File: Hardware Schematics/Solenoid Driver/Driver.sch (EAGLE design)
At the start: 6 parts

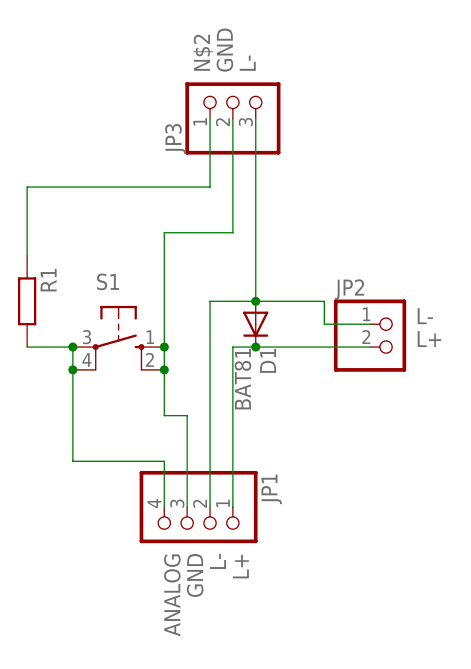
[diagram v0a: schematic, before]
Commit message: New Solenoid Driver Design
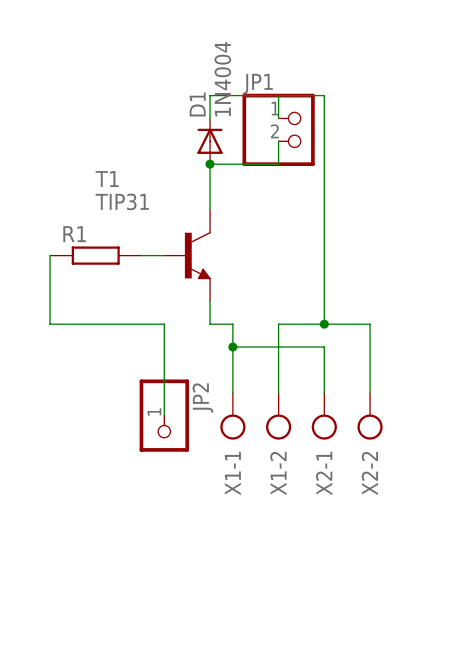
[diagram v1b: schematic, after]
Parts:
- removed JP3: (no value), pinhead:PINHD-1X3
- removed S1: (no value), switch-omron:10-XX
- added T1: TIP31, transistor:TIP31
- added X1, X2: (no value), con-ptr500:AK500/2-H
- D1: value BAT81 -> 1N4004; device diode:BAT81 -> diode:1N4004
- JP1: device pinhead:PINHD-1X4 -> pinhead:PINHD-1X2
- JP2: device pinhead:PINHD-1X2 -> pinhead:PINHD-1X1
- R1: device resistor:R-EU_0204/7 -> rcl:R-EU_0204/2V
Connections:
- removed net ANALOG: JP1.4, R1.2, S1.P, S1.P1
- removed net GND: JP1.3, JP3.2, S1.S, S1.S1
- removed net L+: D1.C, JP1.1, JP2.2
- removed net L-: D1.A, JP1.2, JP2.1, JP3.3
- new net N$1: D1.A, JP1.2, T1.C
- new net N$3: T1.E, X1-1.KL, X2-1.KL
- new net N$4: JP2.1, R1.1
- new net N$5: D1.C, JP1.1, X1-2.KL, X2-2.KL
- net N$2: now also R1.2, T1.B; no longer JP3.1, R1.1
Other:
- moved on the sheet: D1, R1
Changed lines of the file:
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@@
 </classes>
 <parts>
-<part name="S1" library="switch-omron" deviceset="10-XX" device=""/>
-<part name="R1" library="resistor" deviceset="R-EU_" device="0204/7"/>
-<part name="JP1" library="pinhead" deviceset="PINHD-1X4" device=""/>
-<part name="JP2" library="pinhead" deviceset="PINHD-1X2" device=""/>
-<part name="JP3" library="pinhead" deviceset="PINHD-1X3" device=""/>
-<part name="D1" library="diode" deviceset="BAT81" device=""/>
+<part name="T1" library="transistor" deviceset="TIP31" device=""/>
+<part name="R1" library="rcl" deviceset="R-EU_" device="0204/2V"/>
+<part name="D1" library="diode" deviceset="1N4004" device=""/>
+<part name="JP1" library="pinhead" deviceset="PINHD-1X2" device=""/>
+<part name="JP2" library="pinhead" deviceset="PINHD-1X1" device=""/>
+<part name="X1" library="con-ptr500" deviceset="AK500/2-H" device=""/>
+<part name="X2" library="con-ptr500" deviceset="AK500/2-H" device=""/>
 </parts>
 <sheets>
@@
 </plain>
 <instances>
-<instance part="S1" gate="1" x="-5.08" y="45.72" rot="R270"/>
-<instance part="R1" gate="G$1" x="-15.24" y="50.8" rot="R270"/>
-<instance part="JP1" gate="A" x="2.54" y="25.4" rot="R270"/>
-<instance part="JP2" gate="G$1" x="25.4" y="45.72"/>
-<instance part="JP3" gate="A" x="7.62" y="73.66" rot="R90"/>
-<instance part="D1" gate="1" x="10.16" y="48.26" rot="R270"/>
+<instance part="T1" gate="G$1" x="2.54" y="55.88"/>
+<instance part="R1" gate="G$1" x="-7.62" y="55.88"/>
+<instance part="D1" gate="1" x="5.08" y="68.58" rot="R90"/>
+<instance part="JP1" gate="G$1" x="15.24" y="68.58"/>
+<instance part="JP2" gate="G$1" x="0" y="35.56" rot="R270"/>
+<instance part="X1" gate="-1" x="7.62" y="35.56" rot="R90"/>
+<instance part="X1" gate="-2" x="12.7" y="35.56" rot="R90"/>
+<instance part="X2" gate="-1" x="17.78" y="35.56" rot="R90"/>
+<instance part="X2" gate="-2" x="22.86" y="35.56" rot="R90"/>
 </instances>
 <busses>
 </busses>
 <nets>
-<net name="ANALOG" class="0">
+<net name="N$1" class="0">
 <segment>
-<pinref part="R1" gate="G$1" pin="2"/>
-<pinref part="S1" gate="1" pin="P"/>
-<wire x1="-15.24" y1="45.72" x2="-10.16" y2="45.72" width="0.1524" layer="91"/>
-<pinref part="S1" gate="1" pin="P1"/>
-<wire x1="-10.16" y1="45.72" x2="-10.16" y2="43.18" width="0.1524" layer="91"/>
-<wire x1="-10.16" y1="43.18" x2="-10.16" y2="33.02" width="0.1524" layer="91"/>
-<pinref part="JP1" gate="A" pin="4"/>
-<wire x1="-10.16" y1="33.02" x2="0" y2="33.02" width="0.1524" layer="91"/>
-<wire x1="0" y1="33.02" x2="0" y2="27.94" width="0.1524" layer="91"/>
-<label x="0" y="22.86" size="1.778" layer="95" rot="R270"/>
-<junction x="-10.16" y="45.72"/>
-<junction x="-10.16" y="43.18"/>
+<pinref part="D1" gate="1" pin="A"/>
+<pinref part="T1" gate="G$1" pin="C"/>
+<wire x1="5.08" y1="66.04" x2="5.08" y2="60.96" width="0.1524" layer="91"/>
+<pinref part="JP1" gate="G$1" pin="2"/>
+<wire x1="12.7" y1="68.58" x2="12.7" y2="66.04" width="0.1524" layer="91"/>
+<wire x1="12.7" y1="66.04" x2="5.08" y2="66.04" width="0.1524" layer="91"/>
+<junction x="5.08" y="66.04"/>
 </segment>
 </net>
 <net name="N$2" class="0">
 <segment>
-<pinref part="R1" gate="G$1" pin="1"/>
-<wire x1="-15.24" y1="55.88" x2="-15.24" y2="63.5" width="0.1524" layer="91"/>
-<wire x1="-15.24" y1="63.5" x2="5.08" y2="63.5" width="0.1524" layer="91"/>
-<pinref part="JP3" gate="A" pin="1"/>
-<wire x1="5.08" y1="63.5" x2="5.08" y2="71.12" width="0.1524" layer="91"/>
-<label x="5.08" y="76.2" size="1.778" layer="95" rot="R90"/>
+<pinref part="R1" gate="G$1" pin="2"/>
+<pinref part="T1" gate="G$1" pin="B"/>
+<wire x1="-2.54" y1="55.88" x2="0" y2="55.88" width="0.1524" layer="91"/>
 </segment>
 </net>
-<net name="GND" class="0">
+<net name="N$5" class="0">
 <segment>
-<pinref part="S1" gate="1" pin="S"/>
-<pinref part="S1" gate="1" pin="S1"/>
-<wire x1="0" y1="45.72" x2="0" y2="43.18" width="0.1524" layer="91"/>
-<wire x1="0" y1="43.18" x2="0" y2="38.1" width="0.1524" layer="91"/>
-<pinref part="JP1" gate="A" pin="3"/>
-<wire x1="0" y1="38.1" x2="2.54" y2="38.1" width="0.1524" layer="91"/>
-<wire x1="2.54" y1="38.1" x2="2.54" y2="27.94" width="0.1524" layer="91"/>
-<wire x1="0" y1="45.72" x2="0" y2="58.42" width="0.1524" layer="91"/>
-<pinref part="JP3" gate="A" pin="2"/>
-<wire x1="0" y1="58.42" x2="7.62" y2="58.42" width="0.1524" layer="91"/>
-<wire x1="7.62" y1="58.42" x2="7.62" y2="71.12" width="0.1524" layer="91"/>
-<label x="2.54" y="22.86" size="1.778" layer="95" rot="R270"/>
-<label x="7.62" y="76.2" size="1.778" layer="95" rot="R90"/>
-<junction x="0" y="45.72"/>
-<junction x="0" y="43.18"/>
+<pinref part="D1" gate="1" pin="C"/>
+<wire x1="5.08" y1="71.12" x2="5.08" y2="73.66" width="0.1524" layer="91"/>
+<wire x1="5.08" y1="73.66" x2="12.7" y2="73.66" width="0.1524" layer="91"/>
+<wire x1="12.7" y1="73.66" x2="12.7" y2="71.12" width="0.1524" layer="91"/>
+<pinref part="JP1" gate="G$1" pin="1"/>
+<wire x1="12.7" y1="73.66" x2="17.78" y2="73.66" width="0.1524" layer="91"/>
+<wire x1="17.78" y1="73.66" x2="17.78" y2="48.26" width="0.1524" layer="91"/>
+<wire x1="17.78" y1="48.26" x2="12.7" y2="48.26" width="0.1524" layer="91"/>
+<pinref part="X1" gate="-2" pin="KL"/>
+<wire x1="12.7" y1="48.26" x2="12.7" y2="40.64" width="0.1524" layer="91"/>
+<wire x1="17.78" y1="48.26" x2="22.86" y2="48.26" width="0.1524" layer="91"/>
+<pinref part="X2" gate="-2" pin="KL"/>
+<wire x1="22.86" y1="48.26" x2="22.86" y2="40.64" width="0.1524" layer="91"/>
+<junction x="17.78" y="48.26"/>
 </segment>
 </net>
-<net name="L-" class="0">
+<net name="N$4" class="0">
 <segment>
-<pinref part="JP1" gate="A" pin="2"/>
-<wire x1="5.08" y1="27.94" x2="5.08" y2="50.8" width="0.1524" layer="91"/>
-<pinref part="D1" gate="1" pin="A"/>
-<wire x1="5.08" y1="50.8" x2="10.16" y2="50.8" width="0.1524" layer="91"/>
+<pinref part="R1" gate="G$1" pin="1"/>
+<wire x1="-12.7" y1="55.88" x2="-12.7" y2="48.26" width="0.1524" layer="91"/>
+<wire x1="-12.7" y1="48.26" x2="0" y2="48.26" width="0.1524" layer="91"/>
 <pinref part="JP2" gate="G$1" pin="1"/>
-<wire x1="22.86" y1="48.26" x2="17.78" y2="48.26" width="0.1524" layer="91"/>
-<wire x1="17.78" y1="48.26" x2="17.78" y2="50.8" width="0.1524" layer="91"/>
-<wire x1="17.78" y1="50.8" x2="10.16" y2="50.8" width="0.1524" layer="91"/>
-<pinref part="JP3" gate="A" pin="3"/>
-<wire x1="10.16" y1="71.12" x2="10.16" y2="50.8" width="0.1524" layer="91"/>
-<label x="27.94" y="48.26" size="1.778" layer="95"/>
-<label x="5.08" y="22.86" size="1.778" layer="95" rot="R270"/>
-<label x="10.16" y="76.2" size="1.778" layer="95" rot="R90"/>
-<junction x="10.16" y="50.8"/>
+<wire x1="0" y1="48.26" x2="0" y2="38.1" width="0.1524" layer="91"/>
 </segment>
 </net>
-<net name="L+" class="0">
+<net name="N$3" class="0">
 <segment>
-<pinref part="JP1" gate="A" pin="1"/>
-<wire x1="7.62" y1="27.94" x2="7.62" y2="45.72" width="0.1524" layer="91"/>
-<pinref part="D1" gate="1" pin="C"/>
-<wire x1="7.62" y1="45.72" x2="10.16" y2="45.72" width="0.1524" layer="91"/>
-<pinref part="JP2" gate="G$1" pin="2"/>
-<wire x1="10.16" y1="45.72" x2="22.86" y2="45.72" width="0.1524" layer="91"/>
-<label x="27.94" y="45.72" size="1.778" layer="95"/>
-<label x="7.62" y="22.86" size="1.778" layer="95" rot="R270"/>
-<junction x="10.16" y="45.72"/>
+<pinref part="T1" gate="G$1" pin="E"/>
+<wire x1="5.08" y1="50.8" x2="5.08" y2="48.26" width="0.1524" layer="91"/>
+<wire x1="5.08" y1="48.26" x2="7.62" y2="48.26" width="0.1524" layer="91"/>
+<pinref part="X1" gate="-1" pin="KL"/>
+<wire x1="7.62" y1="48.26" x2="7.62" y2="45.72" width="0.1524" layer="91"/>
+<wire x1="7.62" y1="40.64" x2="7.62" y2="45.72" width="0.1524" layer="91"/>
+<wire x1="7.62" y1="45.72" x2="17.78" y2="45.72" width="0.1524" layer="91"/>
+<pinref part="X2" gate="-1" pin="KL"/>
+<wire x1="17.78" y1="45.72" x2="17.78" y2="40.64" width="0.1524" layer="91"/>
+<junction x="7.62" y="45.72"/>
 </segment>
 </net>

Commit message: Updating Repository
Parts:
- removed JP1: (no value), pinhead:PINHD-1X2
- added X3: (no value), con-ptr500:AK500/2-H
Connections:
- net N$3 renamed GND
- net N$1: now also X3-2.KL; no longer JP1.2
- net N$5: now also X3-1.KL; no longer JP1.1
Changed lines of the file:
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@@
 <grid distance="0.1" unitdist="inch" unit="inch" style="lines" multiple="1" display="no" altdistance="0.01" altunitdist="inch" altunit="inch"/>
 <layers>
-<layer number="1" name="Top" color="4" fill="1" visible="yes" active="no"/>
-<layer number="2" name="Route2" color="1" fill="3" visible="yes" active="no"/>
-<layer number="3" name="Route3" color="4" fill="3" visible="yes" active="no"/>
-<layer number="4" name="Route4" color="1" fill="4" visible="yes" active="no"/>
-<layer number="5" name="Route5" color="4" fill="4" visible="yes" active="no"/>
-<layer number="6" name="Route6" color="1" fill="8" visible="yes" active="no"/>
-<layer number="7" name="Route7" color="4" fill="8" visible="yes" active="no"/>
-<layer number="8" name="Route8" color="1" fill="2" visible="yes" active="no"/>
-<layer number="9" name="Route9" color="4" fill="2" visible="yes" active="no"/>
-<layer number="10" name="Route10" color="1" fill="7" visible="yes" active="no"/>
-<layer number="11" name="Route11" color="4" fill="7" visible="yes" active="no"/>
-<layer number="12" name="Route12" color="1" fill="5" visible="yes" active="no"/>
-<layer number="13" name="Route13" color="4" fill="5" visible="yes" active="no"/>
-<layer number="14" name="Route14" color="1" fill="6" visible="yes" active="no"/>
-<layer number="15" name="Route15" color="4" fill="6" visible="yes" active="no"/>
-<layer number="16" name="Bottom" color="1" fill="1" visible="yes" active="no"/>
-<layer number="17" name="Pads" color="2" fill="1" visible="yes" active="no"/>
-<layer number="18" name="Vias" color="2" fill="1" visible="yes" active="no"/>
-<layer number="19" name="Unrouted" color="6" fill="1" visible="yes" active="no"/>
-<layer number="20" name="Dimension" color="15" fill="1" visible="yes" active="no"/>
-<layer number="21" name="tPlace" color="7" fill="1" visible="yes" active="no"/>
-<layer number="22" name="bPlace" color="7" fill="1" visible="yes" active="no"/>
-<layer number="23" name="tOrigins" color="15" fill="1" visible="yes" active="no"/>
-<layer number="24" name="bOrigins" color="15" fill="1" visible="yes" active="no"/>
-<layer number="25" name="tNames" color="7" fill="1" visible="yes" active="no"/>
-<layer number="26" name="bNames" color="7" fill="1" visible="yes" active="no"/>
-<layer number="27" name="tValues" color="7" fill="1" visible="yes" active="no"/>
-<layer number="28" name="bValues" color="7" fill="1" visible="yes" active="no"/>
+<layer number="1" name="Top" color="4" fill="1" visible="no" active="no"/>
+<layer number="2" name="Route2" color="1" fill="3" visible="no" active="no"/>
+<layer number="3" name="Route3" color="4" fill="3" visible="no" active="no"/>
+<layer number="4" name="Route4" color="1" fill="4" visible="no" active="no"/>
+<layer number="5" name="Route5" color="4" fill="4" visible="no" active="no"/>
+<layer number="6" name="Route6" color="1" fill="8" visible="no" active="no"/>
+<layer number="7" name="Route7" color="4" fill="8" visible="no" active="no"/>
+<layer number="8" name="Route8" color="1" fill="2" visible="no" active="no"/>
+<layer number="9" name="Route9" color="4" fill="2" visible="no" active="no"/>
+<layer number="10" name="Route10" color="1" fill="7" visible="no" active="no"/>
+<layer number="11" name="Route11" color="4" fill="7" visible="no" active="no"/>
+<layer number="12" name="Route12" color="1" fill="5" visible="no" active="no"/>
+<layer number="13" name="Route13" color="4" fill="5" visible="no" active="no"/>
+<layer number="14" name="Route14" color="1" fill="6" visible="no" active="no"/>
+<layer number="15" name="Route15" color="4" fill="6" visible="no" active="no"/>
+<layer number="16" name="Bottom" color="1" fill="1" visible="no" active="no"/>
+<layer number="17" name="Pads" color="2" fill="1" visible="no" active="no"/>
+<layer number="18" name="Vias" color="2" fill="1" visible="no" active="no"/>
+<layer number="19" name="Unrouted" color="6" fill="1" visible="no" active="no"/>
+<layer number="20" name="Dimension" color="15" fill="1" visible="no" active="no"/>
+<layer number="21" name="tPlace" color="7" fill="1" visible="no" active="no"/>
+<layer number="22" name="bPlace" color="7" fill="1" visible="no" active="no"/>
+<layer number="23" name="tOrigins" color="15" fill="1" visible="no" active="no"/>
+<layer number="24" name="bOrigins" color="15" fill="1" visible="no" active="no"/>
+<layer number="25" name="tNames" color="7" fill="1" visible="no" active="no"/>
+<layer number="26" name="bNames" color="7" fill="1" visible="no" active="no"/>
+<layer number="27" name="tValues" color="7" fill="1" visible="no" active="no"/>
+<layer number="28" name="bValues" color="7" fill="1" visible="no" active="no"/>
 <layer number="29" name="tStop" color="7" fill="3" visible="no" active="no"/>
 <layer number="30" name="bStop" color="7" fill="6" visible="no" active="no"/>
@@
 <layer number="35" name="tGlue" color="7" fill="4" visible="no" active="no"/>
 <layer number="36" name="bGlue" color="7" fill="5" visible="no" active="no"/>
-<layer number="37" name="tTest" color="7" fill="1" visible="yes" active="no"/>
-<layer number="38" name="bTest" color="7" fill="1" visible="yes" active="no"/>
+<layer number="37" name="tTest" color="7" fill="1" visible="no" active="no"/>
+<layer number="38" name="bTest" color="7" fill="1" visible="no" active="no"/>
 <layer number="39" name="tKeepout" color="4" fill="11" visible="no" active="no"/>
 <layer number="40" name="bKeepout" color="1" fill="11" visible="no" active="no"/>
@@
 <layer number="44" name="Drills" color="7" fill="1" visible="no" active="no"/>
 <layer number="45" name="Holes" color="7" fill="1" visible="no" active="no"/>
-<layer number="46" name="Milling" color="3" fill="1" visible="yes" active="no"/>
-<layer number="47" name="Measures" color="7" fill="1" visible="yes" active="no"/>
-<layer number="48" name="Document" color="7" fill="1" visible="yes" active="no"/>
-<layer number="49" name="Reference" color="7" fill="1" visible="yes" active="no"/>
-<layer number="51" name="tDocu" color="7" fill="1" visible="yes" active="no"/>
-<layer number="52" name="bDocu" color="7" fill="1" visible="yes" active="no"/>
+<layer number="46" name="Milling" color="3" fill="1" visible="no" active="no"/>
+<layer number="47" name="Measures" color="7" fill="1" visible="no" active="no"/>
+<layer number="48" name="Document" color="7" fill="1" visible="no" active="no"/>
+<layer number="49" name="Reference" color="7" fill="1" visible="no" active="no"/>
+<layer number="51" name="tDocu" color="7" fill="1" visible="no" active="no"/>
+<layer number="52" name="bDocu" color="7" fill="1" visible="no" active="no"/>
 <layer number="90" name="Modules" color="5" fill="1" visible="yes" active="yes"/>
 <layer number="91" name="Nets" color="2" fill="1" visible="yes" active="yes"/>
@@
 <part name="R1" library="rcl" deviceset="R-EU_" device="0204/2V"/>
 <part name="D1" library="diode" deviceset="1N4004" device=""/>
-<part name="JP1" library="pinhead" deviceset="PINHD-1X2" device=""/>
 <part name="JP2" library="pinhead" deviceset="PINHD-1X1" device=""/>
 <part name="X1" library="con-ptr500" deviceset="AK500/2-H" device=""/>
 <part name="X2" library="con-ptr500" deviceset="AK500/2-H" device=""/>
+<part name="X3" library="con-ptr500" deviceset="AK500/2-H" device=""/>
 </parts>
 <sheets>
@@
 <instance part="R1" gate="G$1" x="-7.62" y="55.88"/>
 <instance part="D1" gate="1" x="5.08" y="68.58" rot="R90"/>
-<instance part="JP1" gate="G$1" x="15.24" y="68.58"/>
 <instance part="JP2" gate="G$1" x="0" y="35.56" rot="R270"/>
 <instance part="X1" gate="-1" x="7.62" y="35.56" rot="R90"/>
@@
 <instance part="X2" gate="-1" x="17.78" y="35.56" rot="R90"/>
 <instance part="X2" gate="-2" x="22.86" y="35.56" rot="R90"/>
+<instance part="X3" gate="-1" x="17.78" y="71.12" rot="R180"/>
+<instance part="X3" gate="-2" x="17.78" y="66.04" rot="R180"/>
 </instances>
 <busses>
@@
 <pinref part="T1" gate="G$1" pin="C"/>
 <wire x1="5.08" y1="66.04" x2="5.08" y2="60.96" width="0.1524" layer="91"/>
-<pinref part="JP1" gate="G$1" pin="2"/>
-<wire x1="12.7" y1="68.58" x2="12.7" y2="66.04" width="0.1524" layer="91"/>
 <wire x1="12.7" y1="66.04" x2="5.08" y2="66.04" width="0.1524" layer="91"/>
 <junction x="5.08" y="66.04"/>
+<pinref part="X3" gate="-2" pin="KL"/>
 </segment>
 </net>
@@
 <wire x1="5.08" y1="71.12" x2="5.08" y2="73.66" width="0.1524" layer="91"/>
 <wire x1="5.08" y1="73.66" x2="12.7" y2="73.66" width="0.1524" layer="91"/>
-<wire x1="12.7" y1="73.66" x2="12.7" y2="71.12" width="0.1524" layer="91"/>
-<pinref part="JP1" gate="G$1" pin="1"/>
-<wire x1="12.7" y1="73.66" x2="17.78" y2="73.66" width="0.1524" layer="91"/>
-<wire x1="17.78" y1="73.66" x2="17.78" y2="48.26" width="0.1524" layer="91"/>
-<wire x1="17.78" y1="48.26" x2="12.7" y2="48.26" width="0.1524" layer="91"/>
+<wire x1="12.7" y1="73.66" x2="22.86" y2="73.66" width="0.1524" layer="91"/>
+<wire x1="22.86" y1="73.66" x2="22.86" y2="48.26" width="0.1524" layer="91"/>
+<wire x1="22.86" y1="48.26" x2="12.7" y2="48.26" width="0.1524" layer="91"/>
 <pinref part="X1" gate="-2" pin="KL"/>
 <wire x1="12.7" y1="48.26" x2="12.7" y2="40.64" width="0.1524" layer="91"/>
-<wire x1="17.78" y1="48.26" x2="22.86" y2="48.26" width="0.1524" layer="91"/>
 <pinref part="X2" gate="-2" pin="KL"/>
 <wire x1="22.86" y1="48.26" x2="22.86" y2="40.64" width="0.1524" layer="91"/>
-<junction x="17.78" y="48.26"/>
+<junction x="22.86" y="48.26"/>
+<pinref part="X3" gate="-1" pin="KL"/>
+<wire x1="12.7" y1="73.66" x2="12.7" y2="71.12" width="0.1524" layer="91"/>
 </segment>
 </net>
@@
 </segment>
 </net>
-<net name="N$3" class="0">
+<net name="GND" class="0">
 <segment>
 <pinref part="T1" gate="G$1" pin="E"/>
